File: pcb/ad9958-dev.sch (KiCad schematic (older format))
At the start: 88 parts, among them J1 INTERFACE, J2 5V, J3 OUT1, J4 OUT0, U1 AZ1117CH-1.8TRG1, U2 AD9958, U3 LMH6714MF, U4 LMH6714MF, X1 25 MHz

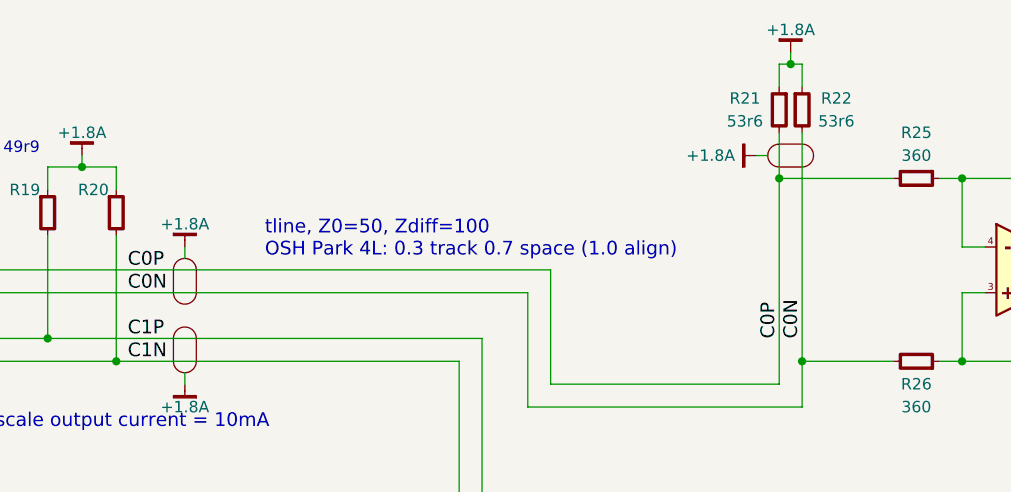
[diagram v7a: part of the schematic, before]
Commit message: Adjusted diff pair routing
Minor PCB appearance tweak
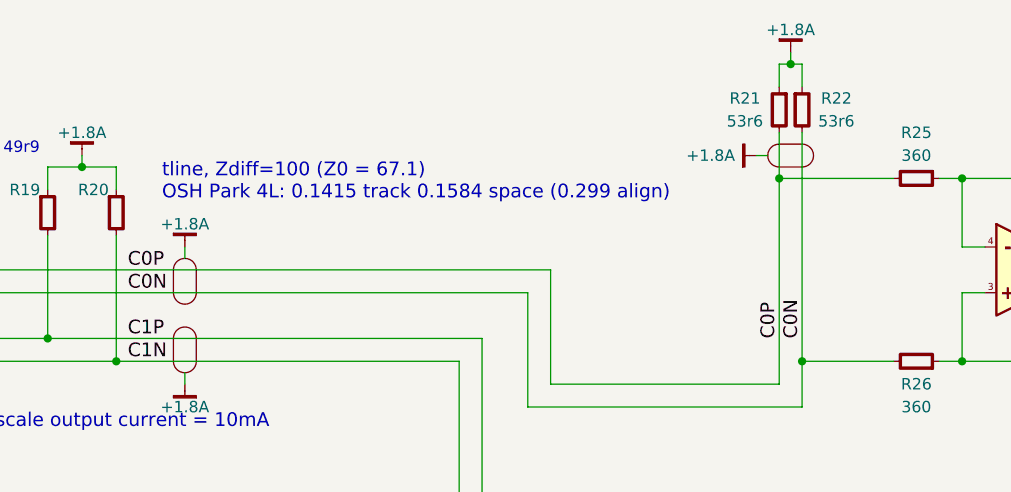
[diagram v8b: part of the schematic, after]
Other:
- note added: "tline, Zdiff=100 (Z0 = 67.1)\nOSH Park 4L: 0.1415 track 0.1584 space (0.299 align)"
- note removed: "tline, Z0=50, Zdiff=100\nOSH Park 4L: 0.3 track 0.7 space (1.0 align)"
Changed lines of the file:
@@
 	1    0    0    -1
 $EndComp
-Text Notes 8100 1650 0    60   ~ 0
-tline, Z0=50, Zdiff=100\nOSH Park 4L: 0.3 track 0.7 space (1.0 align)
+Text Notes 7650 1400 0    60   ~ 0
+tline, Zdiff=100 (Z0 = 67.1)\nOSH Park 4L: 0.1415 track 0.1584 space (0.299 align)
 Text Notes 12350 3250 0    60   ~ 0
 tline, Z0=50
